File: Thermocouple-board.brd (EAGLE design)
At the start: 76.2 x 99.1 mm, 91 parts, among them J1 RJ45, J10 1X2-3.5MM, J11 1X2-3.5MM, J12 1X2-3.5MM, J13 1X2-3.5MM, J2 RJ45, J3 1981584-1, J4 2.1MMJACKTHM, J5 ST-LINK, J6 HEADER-1X3, J7 UART, SW1 PUSHBUTTON, SW2 PUSHBUTTON, U1 STM32F042K6, U10 MAX31855, U11 MAX31855, U12 MAX31855, U13 MAX31855, U20 EEPROM-I2C, U21 EEPROM-I2C, U30 ST3485, U31 ST3485, U40 LP298XS, U70 TPS25921, Y1 8MHz

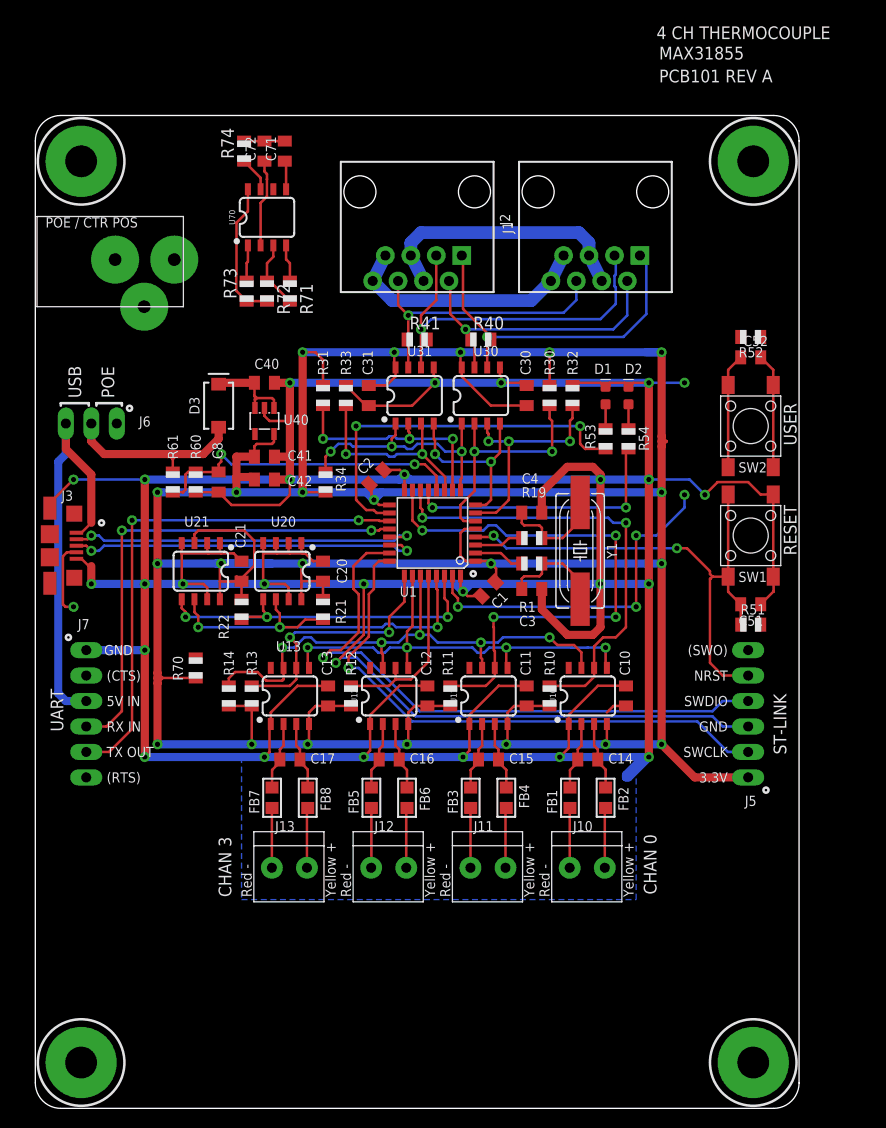
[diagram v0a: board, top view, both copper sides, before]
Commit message: Updated micro USB conn to long pads
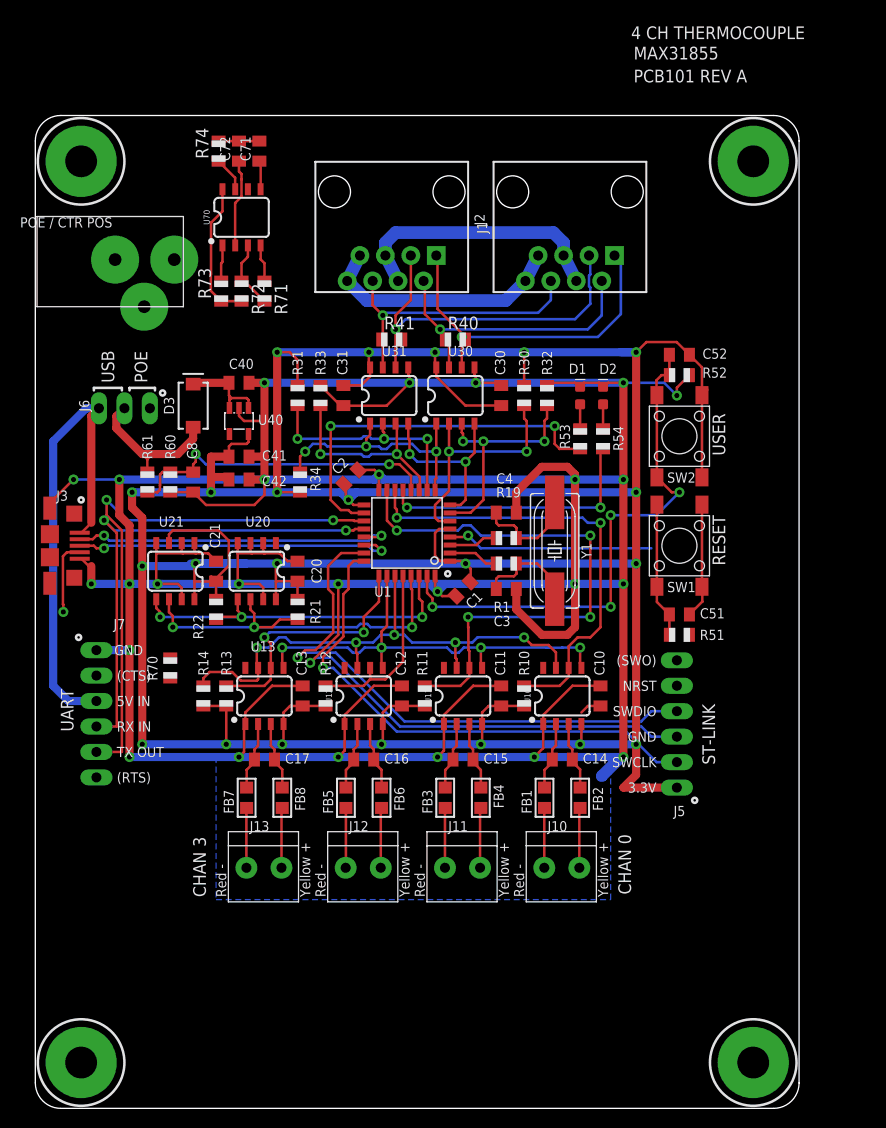
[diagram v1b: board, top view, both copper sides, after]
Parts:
- J3: value 1981584-1 -> 1981584-1LONGPADS; device audio amplifier example:1981584-1 -> Thermocouple-board:1981584-1-LONG
- moved R52 8.07 mm to (64.3, 73.2)
- moved J5 7.18 mm to (64.0, 38.4)
- moved C51 7.18 mm to (64.3, 49.3)
- moved R51 7.18 mm to (64.3, 47.2)
- moved SW1 7.18 mm to (64.3, 56.1)
- moved SW2 7.18 mm to (64.3, 67.1)
- moved C52 7.12 mm to (64.3, 75.2)
- moved J6 3.64 mm to (8.89, 69.8)
- moved C1 2.54 mm to (42.7, 51.8)
- moved C15 2.54 mm to (42.7, 34.8)
- moved FB1 2.54 mm to (50.8, 31.0)
- moved FB6 2.54 mm to (34.5, 31.0)
- moved J11 2.54 mm to (42.7, 24.0)
- moved R40 2.54 mm to (41.9, 76.7)
- moved U11 2.54 mm to (42.7, 41.1)
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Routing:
- net GND: track 578.8 -> 555.7 mm, vias 28 -> 27
- net RST_N: track 53.8 -> 34.2 mm, vias 2 -> 1
- net BTN_USER: track 46.9 -> 54.1 mm
- net USB_VBUS: track 43.2 -> 48.6 mm
- net SWCLK: track 56.3 -> 52.2 mm
- net SWDIO: track 61.1 -> 56.9 mm
- net PWR_IN: track 20.0 -> 16.1 mm
- net USB_DP: track 35.6 -> 32.5 mm
- net USB_DM: track 35.3 -> 32.5 mm
- net UART1_TX: track 52.1 -> 54.9 mm
- net UART1_RX: track 49.0 -> 49.5 mm

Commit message: Mostly routed. Needs connector alignment and hold downs.
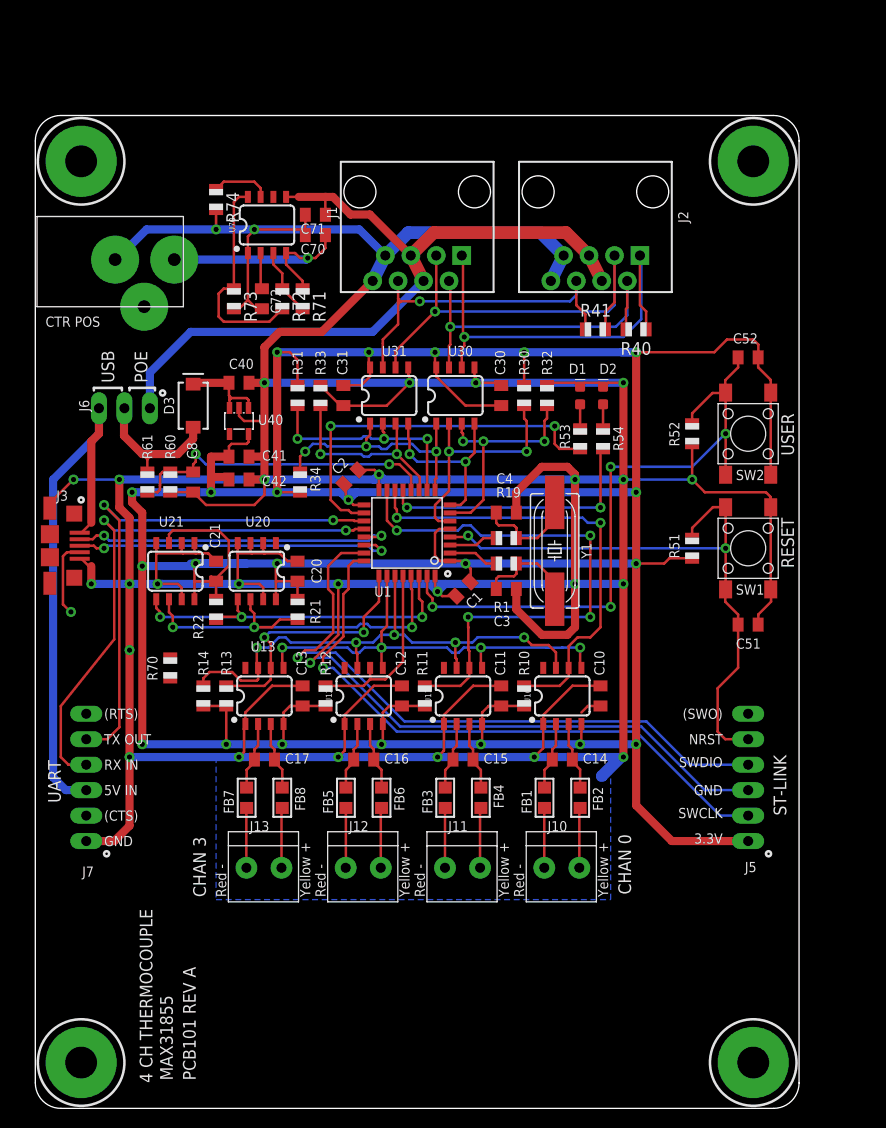
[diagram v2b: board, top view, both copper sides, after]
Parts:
- added C70: 10pF, adafruit:C0805K
- moved R41 20.3 mm to (55.9, 77.7)
- moved R40 18.1 mm to (59.9, 77.7)
- moved C72 14.9 mm to (22.6, 80.8), turned to 270 degrees
- moved J5 8.89 mm to (71.1, 33.0)
- moved R51 8.73 mm to (65.5, 55.9), turned to 90 degrees
- moved C71 8.46 mm to (27.9, 89.2), turned to 180 degrees
- moved C51 6.93 mm to (71.1, 48.3)
- moved C52 6.86 mm to (71.1, 74.9)
- moved SW1 6.86 mm to (71.1, 55.9)
- moved SW2 6.86 mm to (71.1, 67.3)
- moved J7 6.43 mm to (5.08, 33.0), turned to 90 degrees
- moved R52 5.98 mm to (65.5, 67.3), turned to 270 degrees
- moved R74 4.83 mm to (18.0, 90.7), turned to 270 degrees
- moved R72 4.13 mm to (24.6, 80.8)
- moved R71 3.89 mm to (26.7, 80.8)
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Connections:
- net GND: now also C70.2
- net PWR_SRC: now also C70.1
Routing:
- net GND: track 555.7 -> 644.9 mm, vias 27 -> 29
- net POE_PWR: track 29.7 -> 76.7 mm
- net RST_N: track 34.2 -> 60.5 mm, vias 1 -> 2
- net +3V3: track 415.1 -> 436.5 mm
- net PWR_SRC: track 3.72 -> 23.5 mm, vias 0 -> 1
- net BTN_USER: track 54.1 -> 65.4 mm
- net SWCLK: track 52.2 -> 61.5 mm
- net DN_LINK_A: track 35.2 -> 43.9 mm
- net SWDIO: track 56.9 -> 65.4 mm
- net N$24: track 14.1 -> 21.4 mm
- net USB_VBUS: track 48.6 -> 55.9 mm
- net UP_LINK_A: track 37.3 -> 43.7 mm
- net UP_LINK_B: track 28.4 -> 34.6 mm
- net UART1_RX: track 49.5 -> 55.2 mm
- net DN_LINK_B: track 29.8 -> 35.2 mm
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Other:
- board text added: "CTR POS"
- board text removed: "POE / CTR POS"

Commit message: Routing complete
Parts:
- added MH10, MH11, MH12, MH13, MH14, MH15, MH16, MH5, MH6, MH7, MH8, MH9: HOLD_DOWN, Thermocouple-board:HOLD_DOWN
- moved R70 19.4 mm to (26.4, 58.4), turned to 270 degrees
- moved R74 1.44 mm to (17.0, 91.7)
- moved J6 1.27 mm to (7.62, 69.8)
- moved FB1 1.08 mm to (51.6, 31.8)
- moved FB2 1.08 mm to (55.1, 31.8)
- moved C71 1.05 mm to (26.9, 89.4)
- moved C72 1.05 mm to (21.6, 81.0)
- moved R73 1.05 mm to (18.8, 81.0)
- moved U70 1.05 mm to (22.1, 88.4)
- moved C70 1.02 mm to (26.9, 87.1)
- moved FB3 0.92 mm to (41.4, 31.8)
- moved FB4 0.92 mm to (45.0, 31.8)
- moved FB6 0.80 mm to (34.8, 31.8)
- moved FB5 0.80 mm to (31.2, 31.8)
- moved R72 0.80 mm to (23.9, 81.0)
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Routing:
- net UART1_RX: track 55.2 -> 59.9 mm
- net POE_PWR: track 76.7 -> 81.1 mm
- net +3V3: track 436.5 -> 433.9 mm, vias 22 -> 23
- net SPI_SCK: track 44.9 -> 46.7 mm
- net PWR_IN: track 15.4 -> 17.0 mm
- net SPI_CS0_N: track 45.6 -> 44.5 mm
- net GND: track 644.9 -> 645.9 mm
- net PWR_SRC: track 23.5 -> 22.5 mm
- net N$5: track 6.00 -> 6.67 mm
- net N$1: track 5.98 -> 6.62 mm
- net N$7: track 5.98 -> 6.62 mm
- net N$11: track 5.98 -> 6.62 mm
- net N$15: track 5.98 -> 6.62 mm
- net N$12: track 6.82 -> 6.18 mm
- net N$10: track 6.82 -> 6.18 mm
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
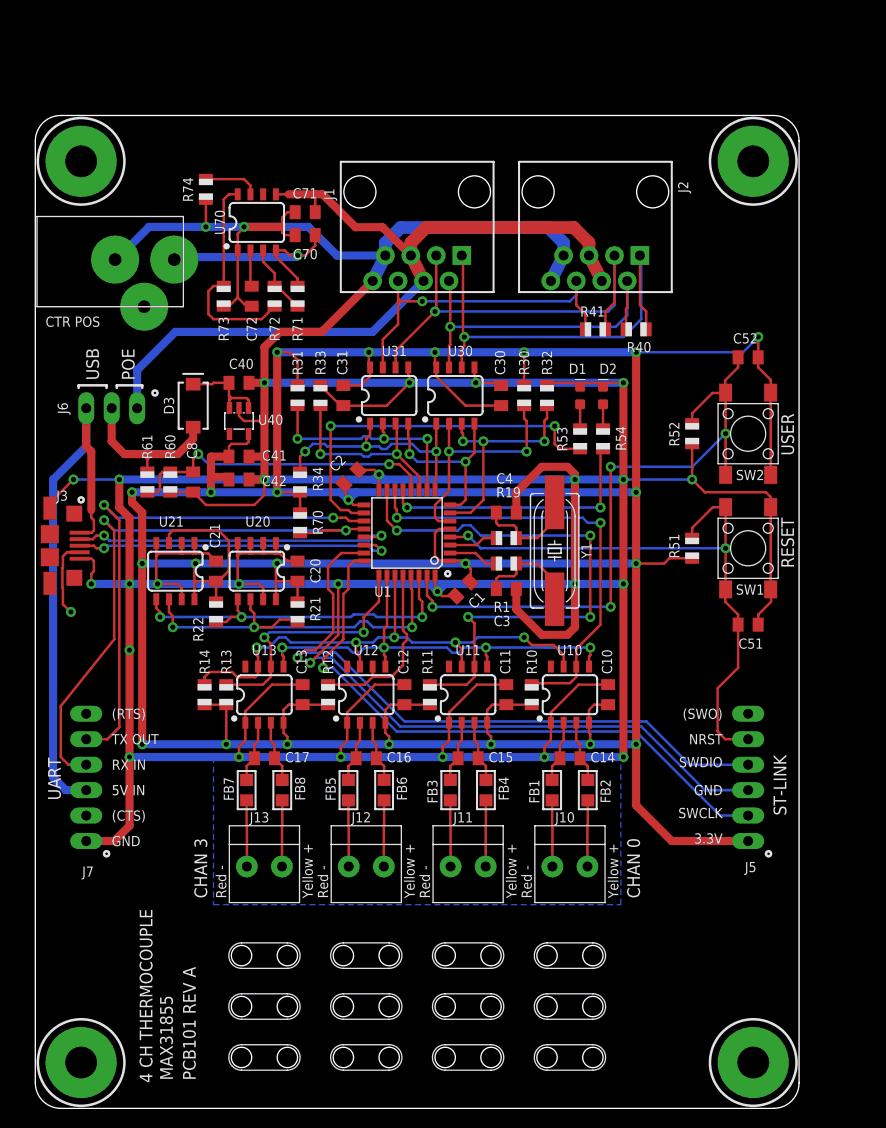
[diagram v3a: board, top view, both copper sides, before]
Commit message: Added ground TPs
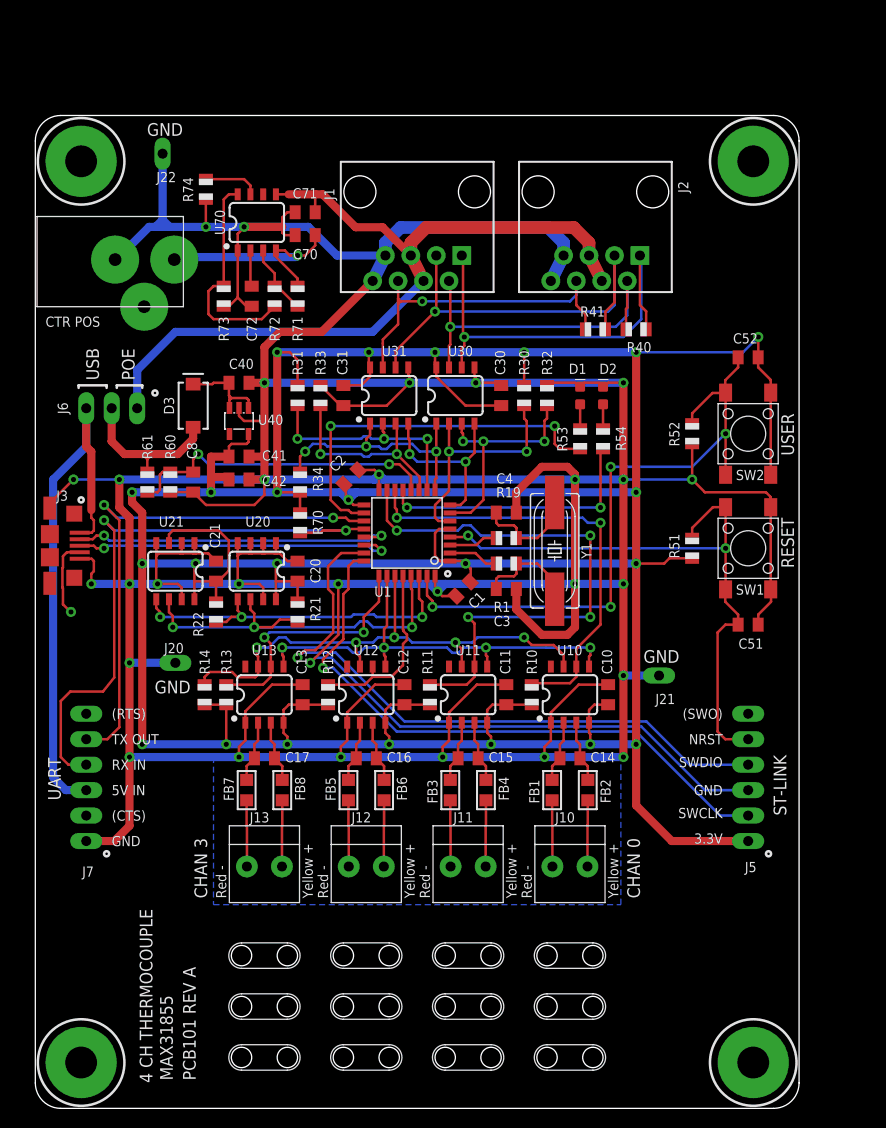
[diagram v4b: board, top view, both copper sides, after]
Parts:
- added J20, J21, J22: HEADER-1X1, Thermocouple-board:1X01_OVAL
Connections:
- net GND: now also J20.1, J21.1, J22.1
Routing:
- net GND: track 645.9 -> 663.4 mm, vias 29 -> 30
- net UART1_RX: track 59.9 -> 62.0 mm
- net RST_N: track 60.5 -> 61.2 mm
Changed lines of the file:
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@@
 <wire x1="8.128" y1="72.136" x2="10.668" y2="72.136" width="0.254" layer="25"/>
 <wire x1="10.668" y1="72.136" x2="10.668" y2="71.882" width="0.254" layer="25"/>
+<text x="64.262" y="45.72" size="1.27" layer="25" font="vector" ratio="15" rot="R180">GND</text>
+<text x="15.494" y="42.672" size="1.27" layer="25" font="vector" ratio="15" rot="R180">GND</text>
+<text x="14.732" y="98.298" size="1.27" layer="25" font="vector" ratio="15" rot="R180">GND</text>
 </plain>
 <attributes>
@@
 </element>
 <element name="R22" library="adafruit" package="R0805" value="10K" x="18.034" y="49.53" smashed="yes" rot="R270">
-<attribute name="NAME" x="15.748" y="49.022" size="1.016" layer="25" font="vector" ratio="15" rot="R270"/>
+<attribute name="NAME" x="15.748" y="49.53" size="1.016" layer="25" font="vector" ratio="15" rot="R270"/>
 <attribute name="VALUE" x="15.748" y="50.292" size="1.27" layer="27" rot="R270"/>
 </element>
@@
 <element name="MH15" library="Thermocouple-board" package="HOLD_DOWN" value="HOLD_DOWN" x="22.86" y="10.16" smashed="yes"/>
 <element name="MH16" library="Thermocouple-board" package="HOLD_DOWN" value="HOLD_DOWN" x="22.86" y="5.08" smashed="yes"/>
+<element name="J20" library="Thermocouple-board" package="1X01_OVAL" value="HEADER-1X1" x="13.97" y="44.45" smashed="yes" rot="R90">
+<attribute name="NAME" x="14.8082" y="46.4312" size="1.016" layer="25" font="vector" ratio="15" rot="R180"/>
+<attribute name="VALUE" x="17.145" y="41.91" size="1.27" layer="27" rot="R90"/>
+</element>
+<element name="J21" library="Thermocouple-board" package="1X01_OVAL" value="HEADER-1X1" x="62.23" y="43.18" smashed="yes" rot="R90">
+<attribute name="NAME" x="63.8302" y="41.3512" size="1.016" layer="25" font="vector" ratio="15" rot="R180"/>
+<attribute name="VALUE" x="65.405" y="40.64" size="1.27" layer="27" rot="R90"/>
+</element>
+<element name="J22" library="Thermocouple-board" package="1X01_OVAL" value="HEADER-1X1" x="12.7" y="95.25" smashed="yes" rot="R180">
+<attribute name="NAME" x="14.0462" y="93.4212" size="1.016" layer="25" font="vector" ratio="15" rot="R180"/>
+<attribute name="VALUE" x="15.24" y="98.425" size="1.27" layer="27" rot="R180"/>
+</element>
 </elements>
 <signals>
@@
 <wire x1="37.211" y1="73.152" x2="37.338" y2="73.025" width="0.254" layer="1"/>
 <via x="9.398" y="35.052" extent="1-16" drill="0.508"/>
-<wire x1="9.398" y1="52.324" x2="9.398" y2="45.72" width="0.8128" layer="1"/>
-<wire x1="9.398" y1="45.72" x2="9.398" y2="35.052" width="0.8128" layer="1"/>
+<wire x1="9.398" y1="52.324" x2="9.398" y2="44.45" width="0.8128" layer="1"/>
+<wire x1="9.398" y1="44.45" x2="9.398" y2="35.052" width="0.8128" layer="1"/>
 <wire x1="9.398" y1="58.928" x2="8.382" y2="59.944" width="0.8128" layer="1"/>
 <wire x1="8.382" y1="62.738" x2="8.382" y2="59.944" width="0.8128" layer="1"/>
@@
 <via x="58.674" y="52.324" extent="1-16" drill="0.508"/>
 <wire x1="50.8" y1="35.052" x2="58.674" y2="35.052" width="0.8128" layer="16"/>
-<wire x1="58.674" y1="52.324" x2="58.674" y2="35.052" width="0.8128" layer="1"/>
+<wire x1="58.674" y1="52.324" x2="58.674" y2="43.18" width="0.8128" layer="1"/>
 <via x="58.674" y="35.052" extent="1-16" drill="0.508"/>
 <via x="53.848" y="52.324" extent="1-16" drill="0.508"/>
+<wire x1="58.674" y1="43.18" x2="58.674" y2="35.052" width="0.8128" layer="1"/>
 <wire x1="20.32" y1="69.88" x2="20.32" y2="69.088" width="0.254" layer="1"/>
 <wire x1="20.32" y1="69.088" x2="20.828" y2="68.58" width="0.254" layer="1"/>
@@
 <wire x1="33.782" y1="62.738" x2="34.798" y2="62.738" width="0.8128" layer="16"/>
 <contactref element="J7" pad="1"/>
-<via x="9.398" y="45.72" extent="1-16" drill="0.508"/>
+<via x="9.398" y="44.45" extent="1-16" drill="0.508"/>
 <wire x1="53.086" y1="64.008" x2="53.848" y2="63.246" width="0.8128" layer="1"/>
 <wire x1="53.848" y1="48.006" x2="53.086" y2="47.244" width="0.8128" layer="1"/>
@@
 <wire x1="27.2434" y1="87.9456" x2="20.828" y2="87.9456" width="0.8128" layer="16"/>
 <wire x1="20.828" y1="87.9456" x2="17.018" y2="87.9456" width="0.8128" layer="16"/>
-<wire x1="17.018" y1="87.9456" x2="11.34538125" y2="87.9456" width="0.8128" layer="16"/>
+<wire x1="17.018" y1="87.9456" x2="13.4004" y2="87.9456" width="0.8128" layer="16"/>
+<wire x1="13.4004" y1="87.9456" x2="12.446" y2="87.9456" width="0.8128" layer="16"/>
+<wire x1="12.446" y1="87.9456" x2="11.9996" y2="87.9456" width="0.8128" layer="16"/>
 <wire x1="8.08178125" y1="84.682" x2="11.34538125" y2="87.9456" width="0.8128" layer="16"/>
 <wire x1="33.655" y1="82.55" x2="34.925" y2="85.09" width="1.27" layer="16"/>
@@
 <wire x1="24.638" y1="87.376" x2="24.638" y2="87.9456" width="0.254" layer="1"/>
 <wire x1="20.32" y1="52.324" x2="12.192" y2="52.324" width="0.8128" layer="16"/>
+<contactref element="J22" pad="1"/>
+<contactref element="J21" pad="1"/>
+<contactref element="J20" pad="1"/>
+<wire x1="62.23" y1="43.18" x2="58.674" y2="43.18" width="0.8128" layer="16"/>
+<via x="58.674" y="43.18" extent="1-16" drill="0.508"/>
+<wire x1="13.97" y1="44.45" x2="9.398" y2="44.45" width="0.8128" layer="16"/>
+<wire x1="12.7" y1="95.25" x2="12.7" y2="88.646" width="0.8128" layer="16"/>
+<wire x1="12.7" y1="88.646" x2="12.7" y2="88.1996" width="0.8128" layer="16"/>
+<wire x1="12.7" y1="88.1996" x2="12.446" y2="87.9456" width="0.8128" layer="16"/>
+<wire x1="11.34538125" y1="87.9456" x2="11.9996" y2="87.9456" width="0.8128" layer="16"/>
+<wire x1="11.9996" y1="87.9456" x2="12.7" y2="88.646" width="0.8128" layer="16"/>
+<wire x1="12.7" y1="88.646" x2="13.4004" y2="87.9456" width="0.8128" layer="16"/>
 </signal>
 <signal name="SPI_CS0_N">
@@
 <wire x1="71.12" y1="36.83" x2="68.834" y2="36.83" width="0.254" layer="1"/>
 <wire x1="68.834" y1="36.83" x2="68.072" y2="37.592" width="0.254" layer="1"/>
-<wire x1="68.072" y1="37.592" x2="68.072" y2="41.91" width="0.254" layer="1"/>
-<wire x1="68.072" y1="41.91" x2="70.12" y2="43.958" width="0.254" layer="1"/>
-<wire x1="70.12" y1="43.958" x2="70.12" y2="48.26" width="0.254" layer="1"/>
+<wire x1="68.85" y1="48.26" x2="70.12" y2="48.26" width="0.254" layer="1"/>
+<wire x1="68.85" y1="48.26" x2="68.072" y2="47.482" width="0.254" layer="1"/>
+<wire x1="68.072" y1="47.482" x2="68.072" y2="37.592" width="0.254" layer="1"/>
 </signal>
 <signal name="SWCLK">
@@
 <contactref element="J7" pad="4"/>
 <via x="6.858" y="58.674" extent="1-16" drill="0.508"/>
-<wire x1="7.874" y1="46.7995" x2="2.54" y2="40.132" width="0.254" layer="1"/>
-<wire x1="2.54" y1="40.132" x2="2.54" y2="35.052" width="0.254" layer="1"/>
+<wire x1="6.752684375" y1="41.587853125" x2="7.874" y2="42.9895" width="0.254" layer="1"/>
 <wire x1="3.302" y1="34.29" x2="5.08" y2="34.29" width="0.254" layer="1"/>
 <wire x1="3.302" y1="34.29" x2="2.54" y2="35.052" width="0.254" layer="1"/>
 <wire x1="6.858" y1="58.674" x2="7.874" y2="57.658" width="0.254" layer="1"/>
-<wire x1="7.874" y1="57.658" x2="7.874" y2="46.7995" width="0.254" layer="1"/>
+<wire x1="7.874" y1="57.658" x2="7.874" y2="42.9895" width="0.254" layer="1"/>
 <contactref element="U1" pad="20"/>
 <wire x1="32.7914" y1="57.804" x2="31.134" y2="57.804" width="0.254" layer="1"/>
@@
 <wire x1="28.464" y1="57.42" x2="28.702" y2="57.658" width="0.254" layer="1"/>
 <wire x1="28.702" y1="57.658" x2="30.988" y2="57.658" width="0.254" layer="1"/>
+<wire x1="2.54" y1="40.64" x2="3.487853125" y2="41.587853125" width="0.254" layer="1"/>
+<wire x1="3.487853125" y1="41.587853125" x2="6.752684375" y2="41.587853125" width="0.254" layer="1"/>
+<wire x1="2.54" y1="35.052" x2="2.54" y2="40.64" width="0.254" layer="1"/>
 </signal>
 <signal name="N$2">
